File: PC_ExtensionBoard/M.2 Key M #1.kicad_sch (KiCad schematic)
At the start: 16 parts, among them J8 Bus_M.2_1-2199230-6

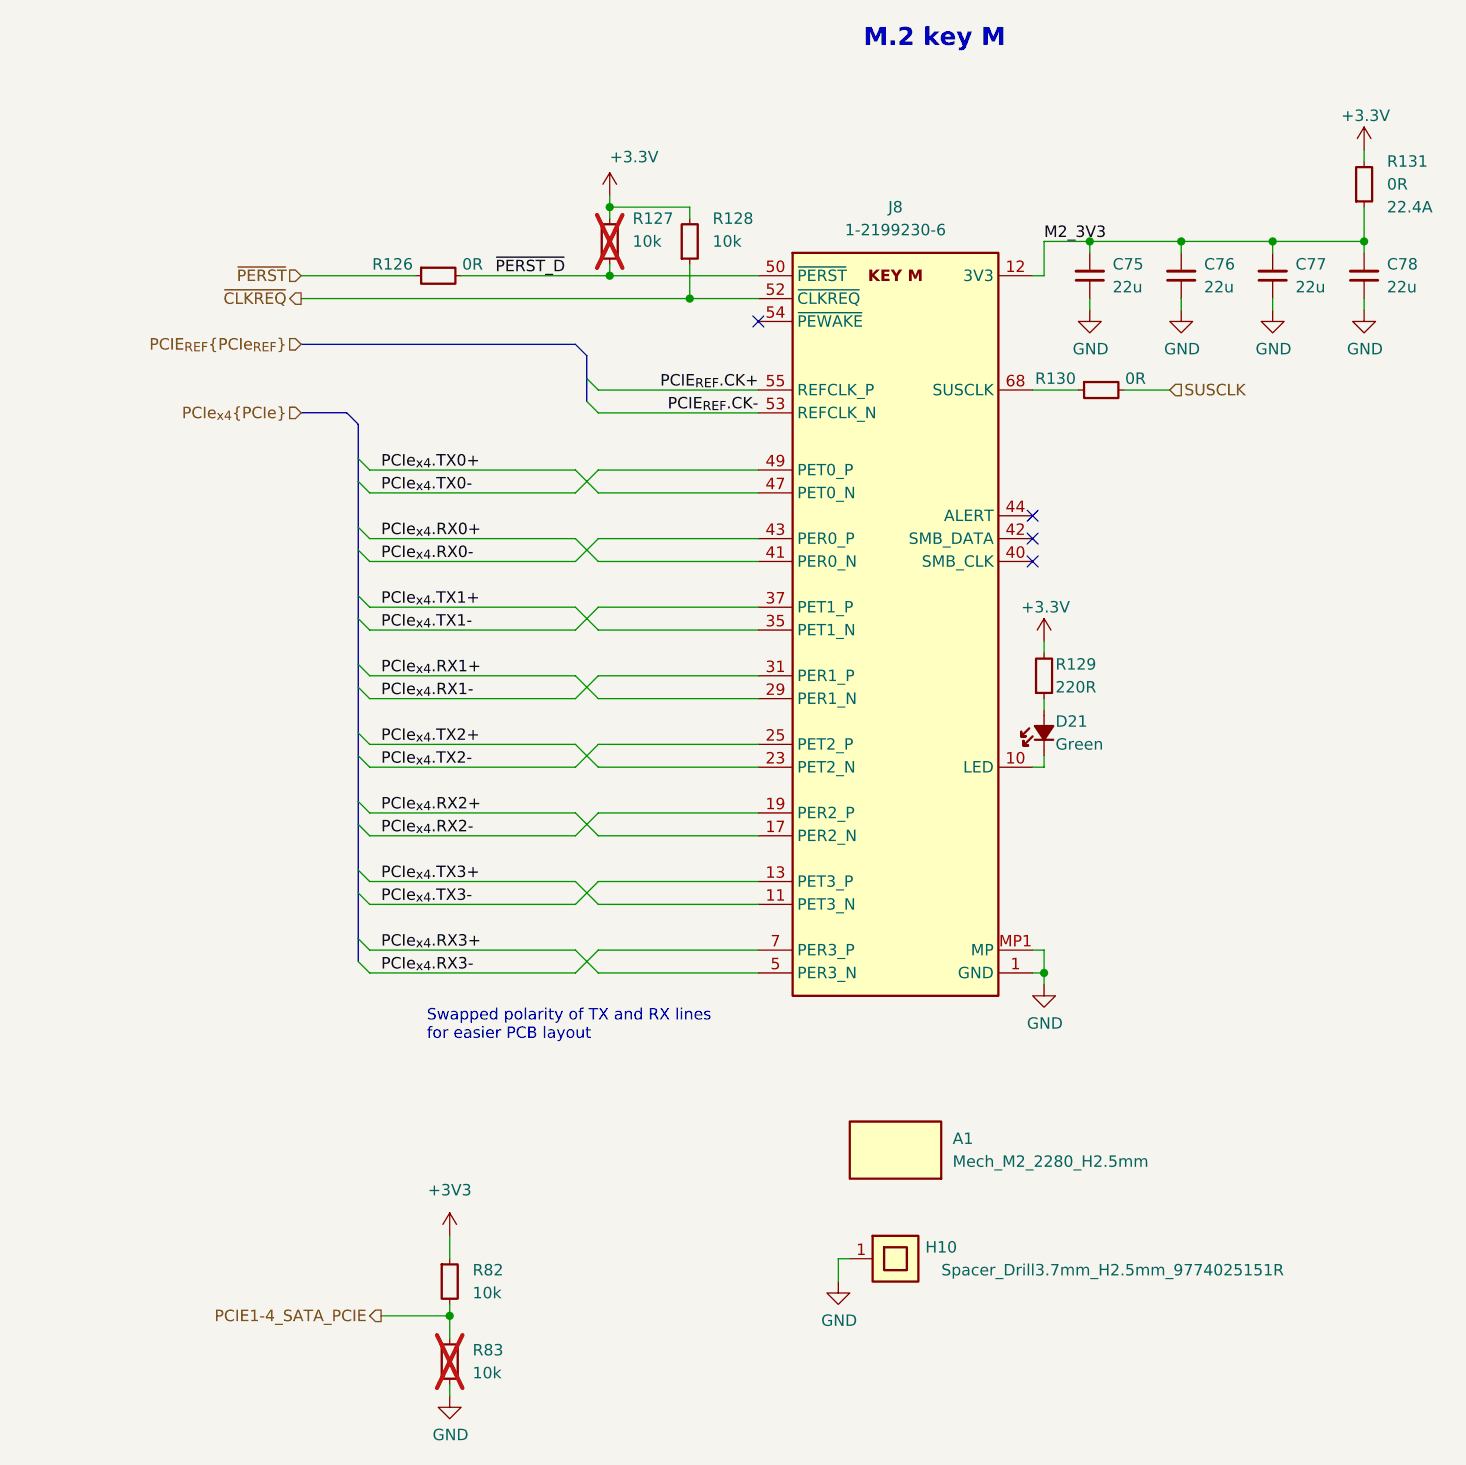
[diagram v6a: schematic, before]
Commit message: attempts with impedance control
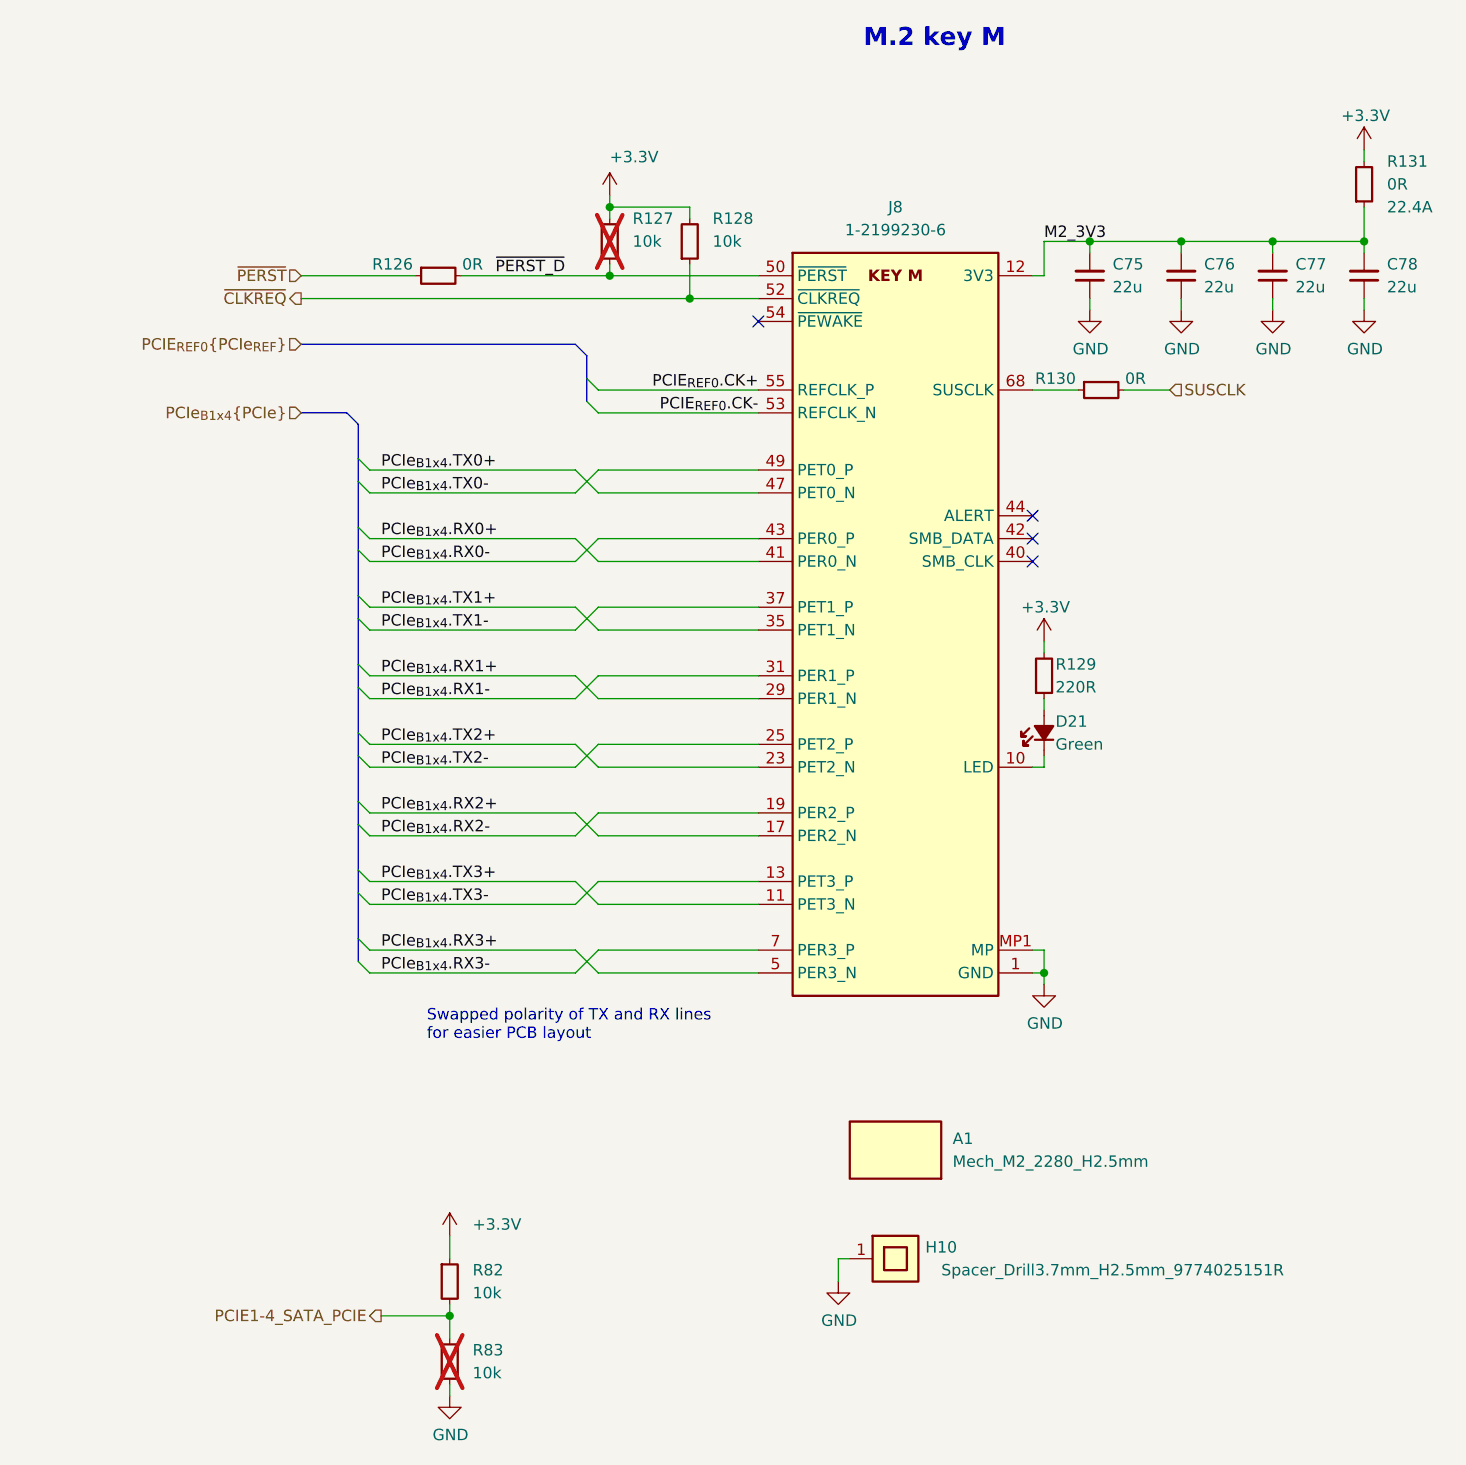
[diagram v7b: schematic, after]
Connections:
- net +3V3 is gone; now on net +3.3V: R82.1
- net PCIE_{REF}.CK+ renamed PCIE_{REF0}.CK+
- net PCIE_{REF}.CK- renamed PCIE_{REF0}.CK-
- net PCIe_{x4}.RX0+ renamed PCIe_{B1x4}.RX0+
- net PCIe_{x4}.RX0- renamed PCIe_{B1x4}.RX0-
- net PCIe_{x4}.RX1+ renamed PCIe_{B1x4}.RX1+
- net PCIe_{x4}.RX1- renamed PCIe_{B1x4}.RX1-
- net PCIe_{x4}.RX2+ renamed PCIe_{B1x4}.RX2+
- net PCIe_{x4}.RX2- renamed PCIe_{B1x4}.RX2-
- net PCIe_{x4}.RX3+ renamed PCIe_{B1x4}.RX3+
- net PCIe_{x4}.RX3- renamed PCIe_{B1x4}.RX3-
- net PCIe_{x4}.TX0+ renamed PCIe_{B1x4}.TX0+
- net PCIe_{x4}.TX0- renamed PCIe_{B1x4}.TX0-
- net PCIe_{x4}.TX1+ renamed PCIe_{B1x4}.TX1+
- net PCIe_{x4}.TX1- renamed PCIe_{B1x4}.TX1-
- net PCIe_{x4}.TX2+ renamed PCIe_{B1x4}.TX2+
- net PCIe_{x4}.TX2- renamed PCIe_{B1x4}.TX2-
- net PCIe_{x4}.TX3+ renamed PCIe_{B1x4}.TX3+
- net PCIe_{x4}.TX3- renamed PCIe_{B1x4}.TX3-
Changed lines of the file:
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@@
 		)
 	)
-	(label "PCIe_{x4}.TX2+"
+	(label "PCIe_{B1x4}.TX2+"
 		(at 68.58 105.41 0)
 		(effects
@@
 		)
 	)
-	(label "PCIe_{x4}.TX3-"
+	(label "PCIe_{B1x4}.TX3-"
 		(at 68.58 123.19 0)
 		(effects
@@
 		)
 	)
-	(label "PCIe_{x4}.RX3-"
+	(label "PCIe_{B1x4}.RX3-"
 		(at 68.58 130.81 0)
 		(effects
@@
 		)
 	)
-	(label "PCIe_{x4}.RX2+"
+	(label "PCIe_{B1x4}.RX2+"
 		(at 68.58 113.03 0)
 		(effects
@@
 		)
 	)
-	(label "PCIe_{x4}.RX0+"
+	(label "PCIe_{B1x4}.RX0+"
 		(at 68.58 82.55 0)
 		(effects
@@
 		)
 	)
-	(label "PCIE_{REF}.CK+"
+	(label "PCIE_{REF0}.CK+"
 		(at 110.49 66.04 180)
 		(effects
@@
 		)
 	)
-	(label "PCIe_{x4}.TX1+"
+	(label "PCIe_{B1x4}.TX1+"
 		(at 68.58 90.17 0)
 		(effects
@@
 		)
 	)
-	(label "PCIe_{x4}.TX3+"
+	(label "PCIe_{B1x4}.TX3+"
 		(at 68.58 120.65 0)
 		(effects
@@
 		)
 	)
-	(label "PCIe_{x4}.TX2-"
+	(label "PCIe_{B1x4}.TX2-"
 		(at 68.58 107.95 0)
 		(effects
@@
 		)
 	)
-	(label "PCIe_{x4}.TX0-"
+	(label "PCIe_{B1x4}.TX0-"
 		(at 68.58 77.47 0)
 		(effects
@@
 		)
 	)
-	(label "PCIe_{x4}.RX3+"
+	(label "PCIe_{B1x4}.RX3+"
 		(at 68.58 128.27 0)
 		(effects
@@
 		)
 	)
-	(label "PCIe_{x4}.RX0-"
+	(label "PCIe_{B1x4}.RX0-"
 		(at 68.58 85.09 0)
 		(effects
@@
 		)
 	)
-	(label "PCIe_{x4}.TX1-"
+	(label "PCIe_{B1x4}.TX1-"
 		(at 68.58 92.71 0)
 		(effects
@@
 		)
 	)
-	(label "PCIE_{REF}.CK-"
+	(label "PCIE_{REF0}.CK-"
 		(at 110.49 68.58 180)
 		(effects
@@
 		)
 	)
-	(label "PCIe_{x4}.RX2-"
+	(label "PCIe_{B1x4}.RX2-"
 		(at 68.58 115.57 0)
 		(effects
@@
 		)
 	)
-	(label "PCIe_{x4}.TX0+"
+	(label "PCIe_{B1x4}.TX0+"
 		(at 68.58 74.93 0)
 		(effects
@@
 		)
 	)
-	(label "PCIe_{x4}.RX1+"
+	(label "PCIe_{B1x4}.RX1+"
 		(at 68.58 97.79 0)
 		(effects
@@
 		)
 	)
-	(label "PCIe_{x4}.RX1-"
+	(label "PCIe_{B1x4}.RX1-"
 		(at 68.58 100.33 0)
 		(effects
@@
 		)
 	)
-	(hierarchical_label "PCIE_{REF}{PCIe_{REF}}"
+	(hierarchical_label "PCIE_{REF0}{PCIe_{REF}}"
 		(shape input)
 		(at 59.69 60.96 180)
@@
 		)
 	)
-	(hierarchical_label "PCIe_{x4}{PCIe}"
+	(hierarchical_label "PCIe_{B1x4}{PCIe}"
 		(shape input)
 		(at 59.69 68.58 180)
@@
 			)
 		)
-		(property "Value" "+3V3"
-			(at 76.2 154.94 0)
+		(property "Value" "+3.3V"
+			(at 78.74 158.7499 0)
 			(show_name no)
 			(do_not_autoplace no)
@@
 					(size 1.27 1.27)
 				)
+				(justify left)
 			)
 		)

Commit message: bug fixes
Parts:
- J8: LCSC (none) -> C4710843
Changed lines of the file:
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@@
+			)
+		)
+		(property "LCSC" "C4710843"
+			(at 110.49 53.34 0)
+			(hide yes)
+			(show_name no)
+			(do_not_autoplace no)
+			(effects
+				(font
+					(size 1.27 1.27)
+				)
 			)
 		)
